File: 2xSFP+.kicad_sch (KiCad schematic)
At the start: 55 parts, among them J2 SFP+_Bel_SS-79100-010, U5 PCA9539AHF

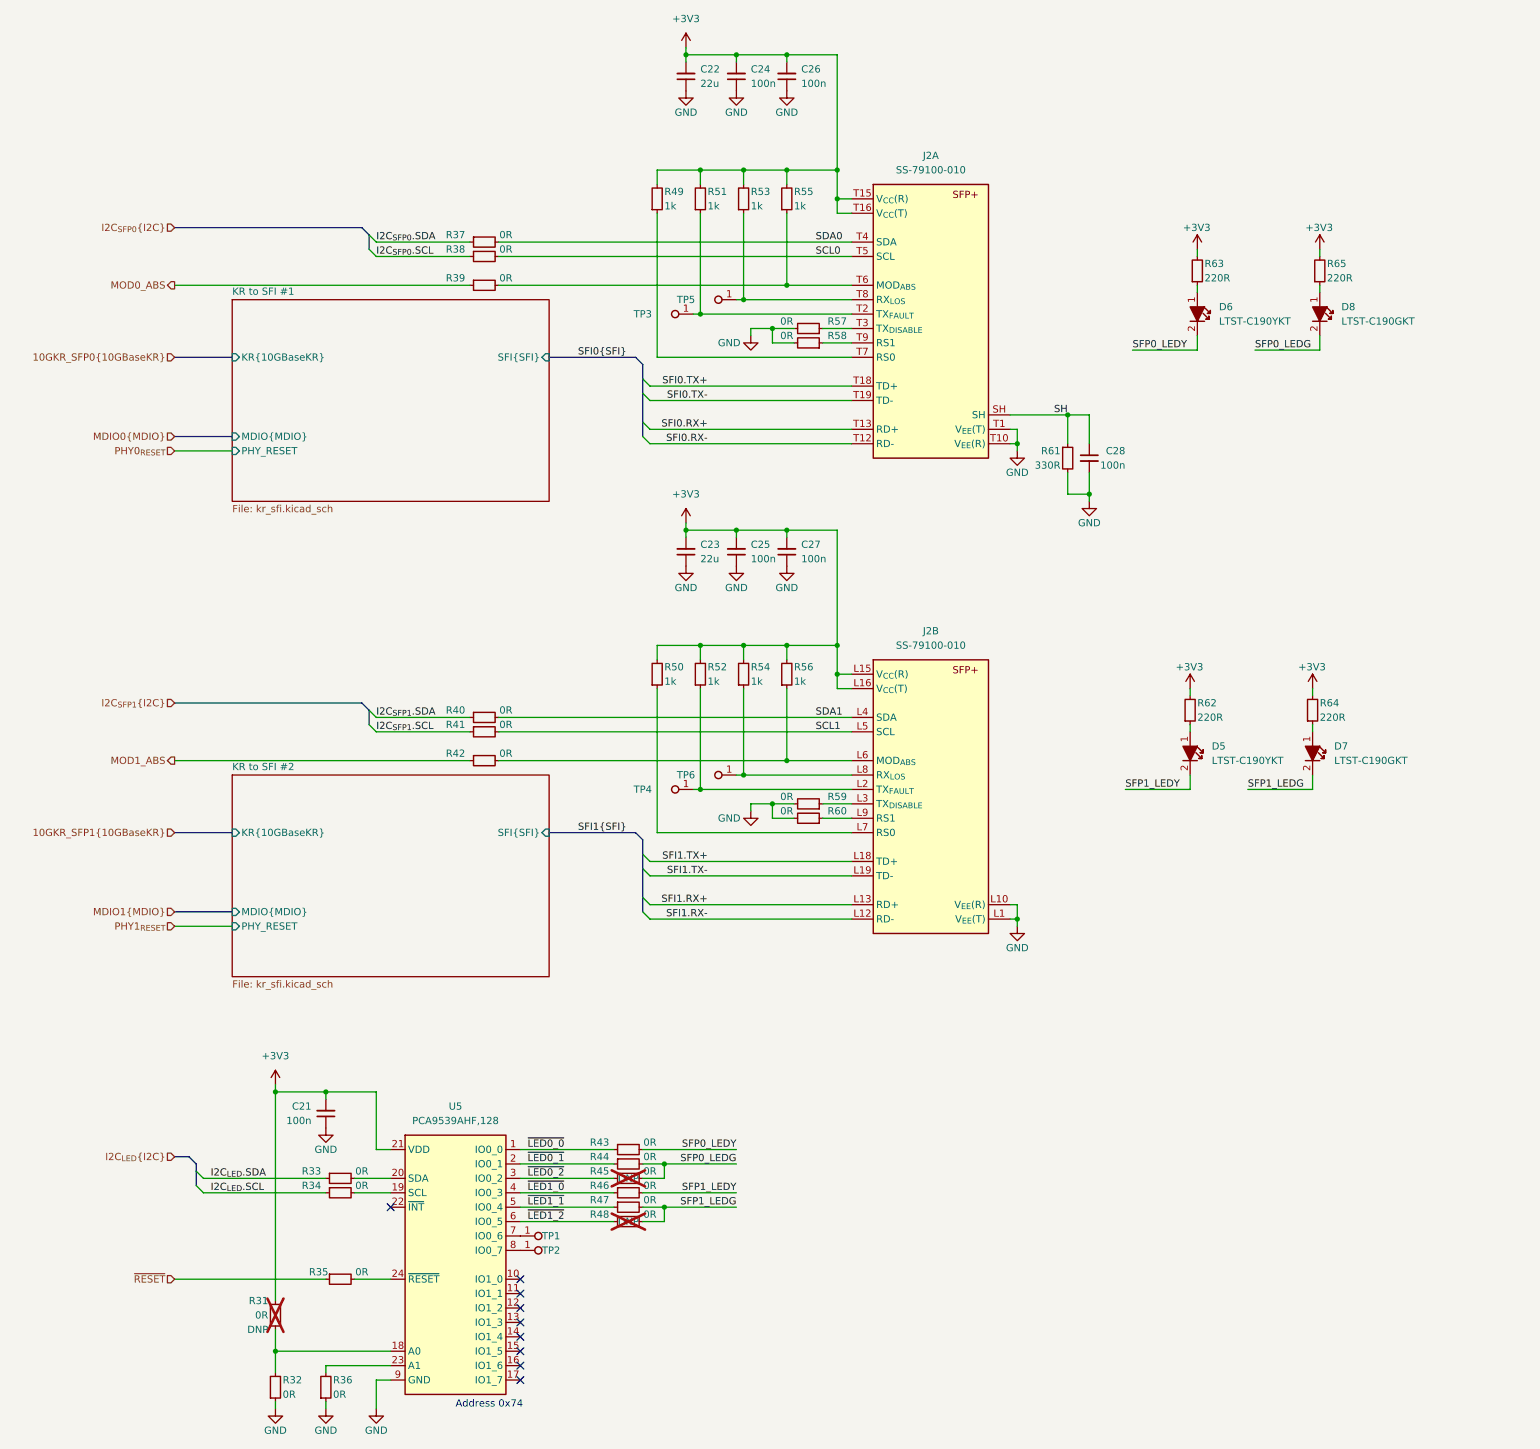
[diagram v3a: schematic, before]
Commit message: Update components from the library
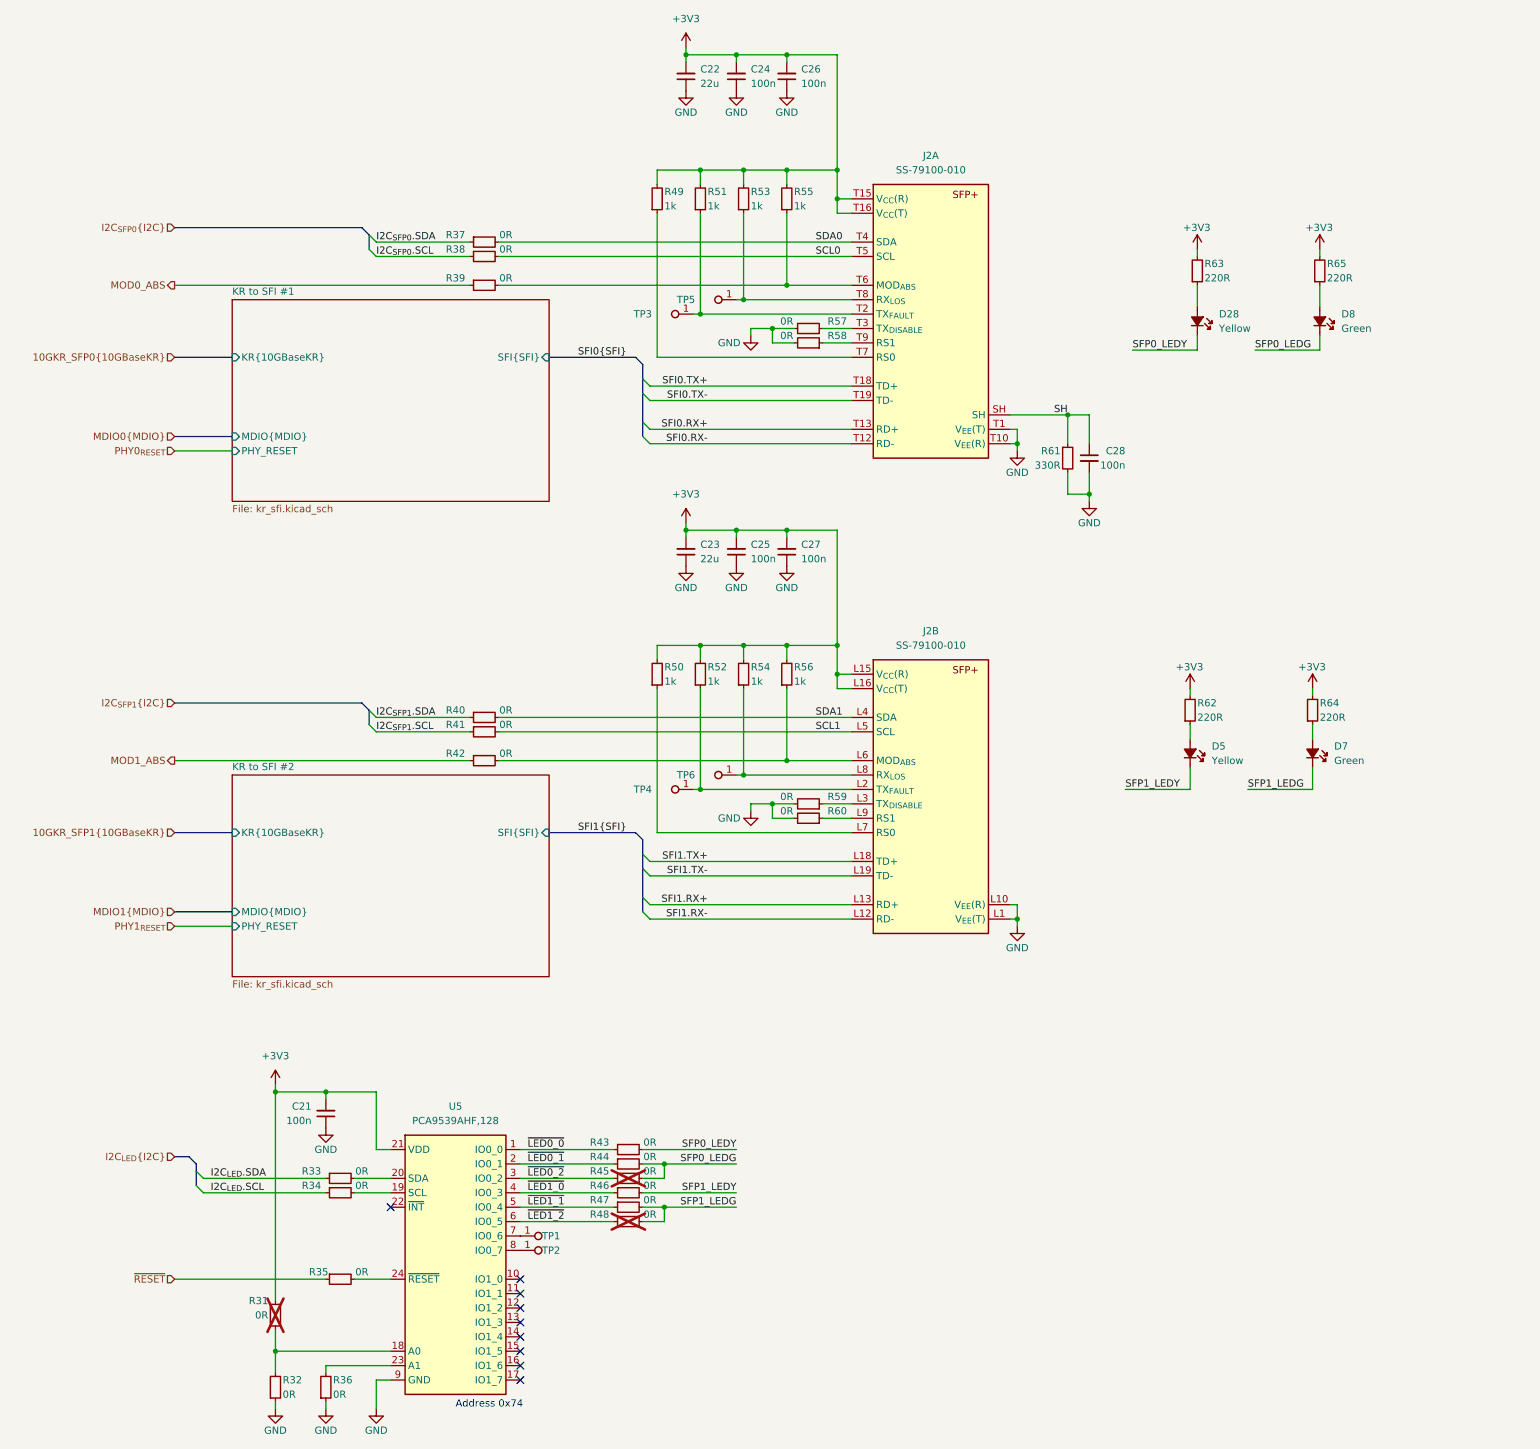
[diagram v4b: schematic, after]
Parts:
- removed D5, D6: LED_Y_0603_LTST-C190YKT, antmicro-footprints:LED_0603_1608Metric_G, symbol antmicroLEDIndicationDiscrete:LED_Y_0603_LTST-C190YKT
- removed J2: SFP+_Bel_SS-79100-010, antmicro-footprints:SFP+_SS-79100-010, symbol antmicroEdgeConnectors:SFP+_Bel_SS-79100-010
- added D28, D5: LED_Y_0402_VLMY1500-GS08, antmicro-footprints:LED_0402_1005Metric_Y, symbol antmicroLEDIndicationDiscrete:LED_Y_0402_VLMY1500-GS08
- added J2: Bel-Fuse_SFP+_2x20_SS-79100-010, antmicro-footprints:Conn_Bel-Fuse_SFP+_2x20_SS-79100-010, symbol antmicroWire2BoardConnectors:Bel-Fuse_SFP+_2x20_SS-79100-010
- C21, C22, C23, C24, C25, C26, C27, C28, R32, R33, R34, R35, R36, R37, R38, R39, R40, R41, R42, R43, R44, R46, R47, R49, R50, R51, R52, R53, R54, R55, R56, R57, R58, R59, R60, R61, R62, R63, R64, R65, TP1, TP2, TP3, TP4, TP5, TP6: Public (none) -> False
- D7, D8: Color (none) -> Green; Manufacturer Lite-On Inc. -> Lite-On; Public (none) -> False
- R31: DNP DNP -> (none); Public (none) -> False
- R45, R48: Public (none) -> False; dnp DNP -> (none)
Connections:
- net +3V3: now also J2.L15 (V_{CC}(R)), J2.L16 (V_{CC}(T)), J2.T15 (V_{CC}(R)), J2.T16 (V_{CC}(T))
- net GND: now also J2.L1 (V_{EE}(T)), J2.L10 (V_{EE}(R)), J2.L11 (V_{EE}(R)), J2.L14 (V_{EE}(R)), J2.L17 (V_{EE}(T)), J2.L20 (V_{EE}(T)), J2.T1 (V_{EE}(T)), J2.T10 (V_{EE}(R)), J2.T11 (V_{EE}(R)), J2.T14 (V_{EE}(R)), J2.T17 (V_{EE}(T)), J2.T20 (V_{EE}(T))
- net SCL0: now also J2.T5 (SCL)
- net SCL1: now also J2.L5 (SCL)
- net SDA0: now also J2.T4 (SDA)
- net SDA1: now also J2.L4 (SDA)
- net SFI0.RX+: now also J2.T13 (RD+)
- net SFI0.RX-: now also J2.T12 (RD-)
- net SFI0.TX+: now also J2.T18 (TD+)
- net SFI0.TX-: now also J2.T19 (TD-)
- net SFI1.RX+: now also J2.L13 (RD+)
- net SFI1.RX-: now also J2.L12 (RD-)
- net SFI1.TX+: now also J2.L18 (TD+)
- net SFI1.TX-: now also J2.L19 (TD-)
- net SFP0_LEDG: now also D8.1 (C); no longer D8.2
- net SFP0_LEDY: now also D28.1 (C)
- net SFP1_LEDG: now also D7.1 (C); no longer D7.2
- net SFP1_LEDY: now also D5.1 (C)
- net SH: now also J2.SH
- net at R51.1, TP3.1: now also J2.T2 (TX_{FAULT})
- net at R57.1: now also J2.T3 (TX_{DISABLE})
- net at R39.2, R55.1: now also J2.T6 (MOD_{ABS})
- net at R49.1: now also J2.T7 (RS0)
- net at R53.1, TP5.1: now also J2.T8 (RX_{LOS})
- net at R58.1: now also J2.T9 (RS1)
- net at R42.2, R56.1: now also J2.L6 (MOD_{ABS})
- net at R63.1: now also D28.2 (A)
- net at R52.1, TP4.1: now also J2.L2 (TX_{FAULT})
- net at R59.1: now also J2.L3 (TX_{DISABLE})
- net at R50.1: now also J2.L7 (RS0)
- net at R54.1, TP6.1: now also J2.L8 (RX_{LOS})
- net at R60.1: now also J2.L9 (RS1)
- net at R62.1: now also D5.2 (A)
- net at R65.1: now also D8.2 (A); no longer D8.1
- net at R64.1: now also D7.2 (A); no longer D7.1
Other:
- moved on the sheet: D7, D8

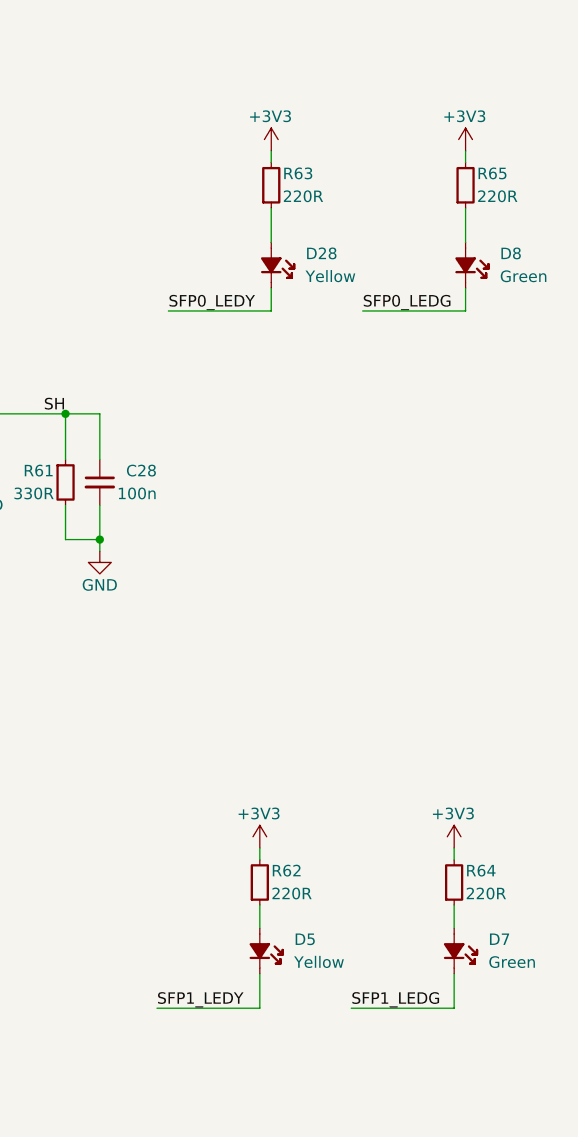
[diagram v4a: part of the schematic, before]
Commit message: [#66234] Layout OCuLink power, SFP, low speed signals
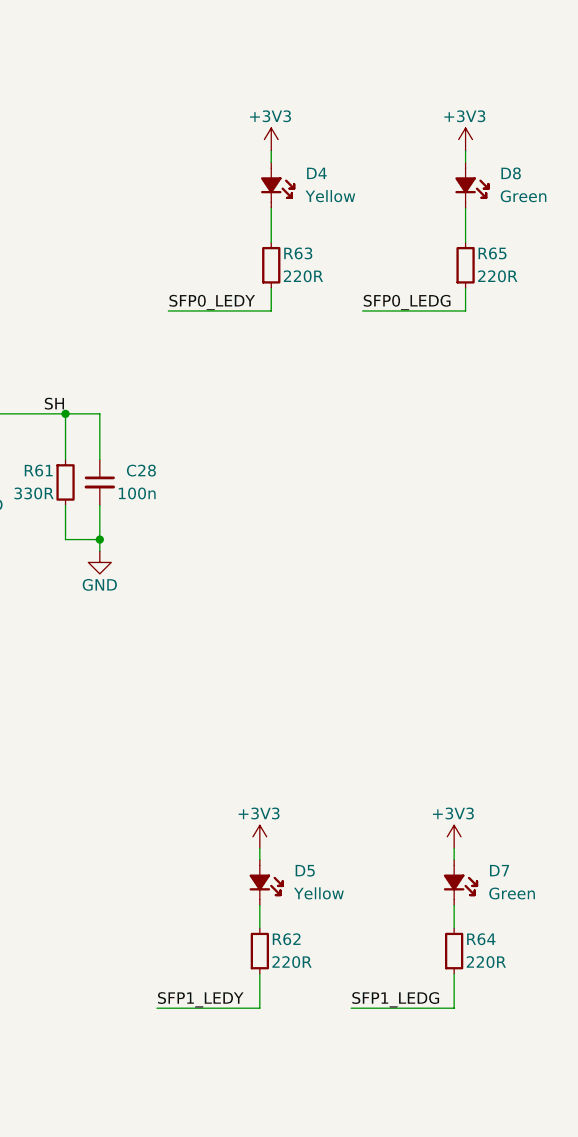
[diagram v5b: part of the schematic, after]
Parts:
- removed D28: LED_Y_0402_VLMY1500-GS08, antmicro-footprints:LED_0402_1005Metric_Y, symbol antmicroLEDIndicationDiscrete:LED_Y_0402_VLMY1500-GS08
- added D4: LED_Y_0402_VLMY1500-GS08, antmicro-footprints:LED_0402_1005Metric_Y, symbol antmicroLEDIndicationDiscrete:LED_Y_0402_VLMY1500-GS08
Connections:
- net +3V3: now also D5.2 (A), D7.2 (A), D8.2 (A), D4.2 (A); no longer R62.2, R63.2, R64.2, R65.2
- net SFP0_LEDG: now also R65.1; no longer D8.1 (C)
- net SFP0_LEDY: now also R63.1
- net SFP1_LEDG: now also R64.1; no longer D7.1 (C)
- net SFP1_LEDY: now also R62.1; no longer D5.1 (C)
- new net: D7.1 (C), R64.2
- new net: D4.1 (C), R63.2
- new net: D5.1 (C), R62.2
- new net: D8.1 (C), R65.2
